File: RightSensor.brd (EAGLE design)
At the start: 19.7 x 19.7 mm, 9 parts

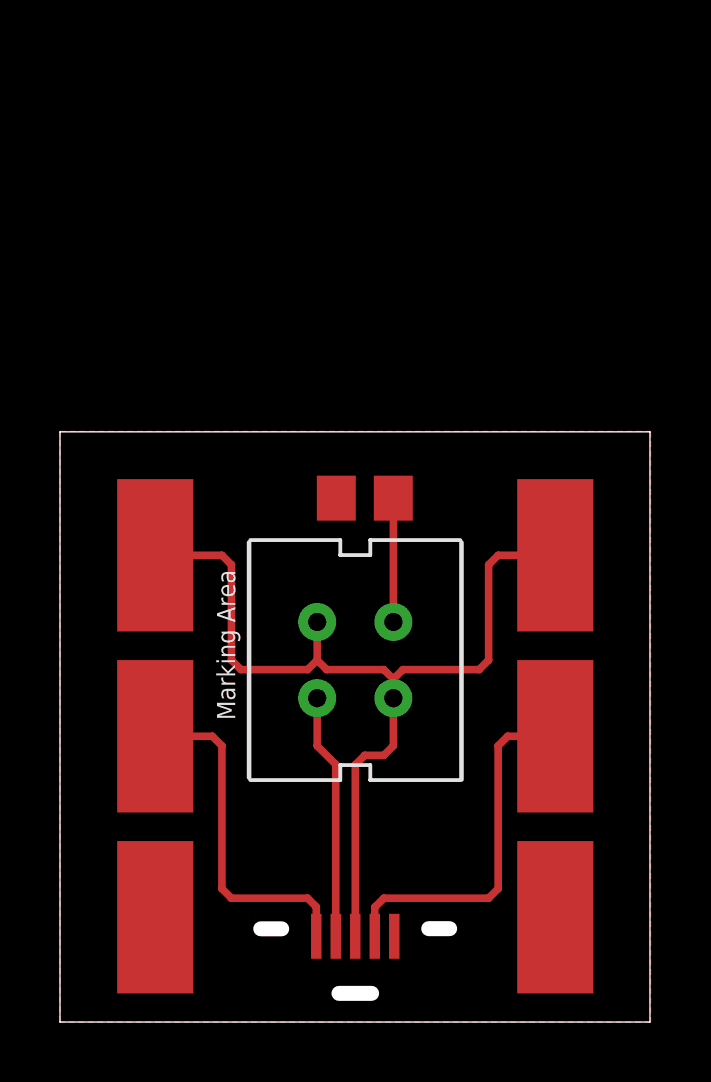
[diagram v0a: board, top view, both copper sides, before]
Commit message: Added sensor boards, started on proto frame design
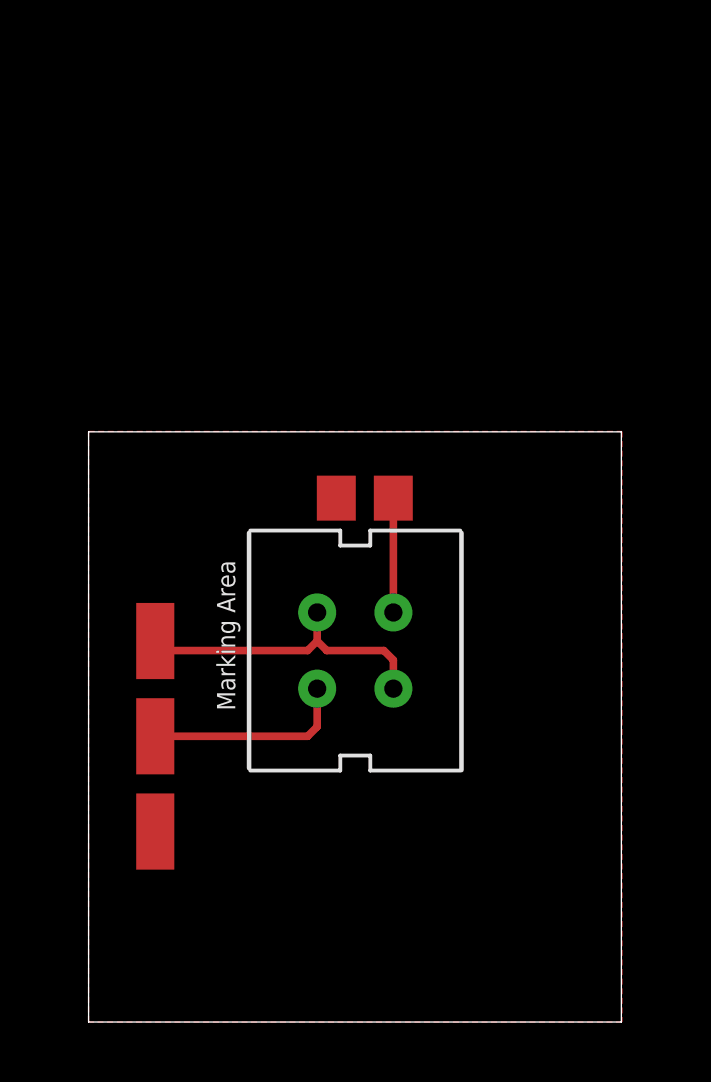
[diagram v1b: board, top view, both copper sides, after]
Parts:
- removed PAD4, PAD5, PAD6: WIREPADSMD2,54-5,08, wirepad:SMD2,54-5,08
- removed U$1: MOLES-USB-MICRO, tom:MOLEX-USB-MICRO
- removed U$2: CNY70, cny70:4
- added X2: CNY70, cny70:4
- PAD1, PAD2, PAD3: value WIREPADSMD2,54-5,08 -> WIREPADSMD1,27-254; device wirepad:SMD2,54-5,08 -> wirepad:SMD1,27-2,54
- moved PAD1 2.86 mm to (1.91, 12.7)
- moved PAD3 2.86 mm to (1.91, 6.35)
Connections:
- removed net SENSOR1: PAD2.1, U$1.VBUS
- removed net SENSOR2: U$1.D-, U$2.E
- removed net SENSOR3: PAD5.1, U$1.ID
- new net SENSOR: PAD2.1, X2.E
- net GND: no longer PAD6.1, U$1.GND
- net N$1: now also X2.K; no longer U$2.K
- net VCC: now also X2.A, X2.C; no longer PAD4.1, U$1.D+, U$2.A, U$2.C
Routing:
- net VCC: track 31.5 -> 10.4 mm
- net SENSOR3: track 12.1 -> 0.00 mm
- net SENSOR1: track 11.5 -> 0.00 mm
- net SENSOR2: track 8.19 -> 0.00 mm
- net SENSOR: track 0.00 -> 6.80 mm
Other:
- board size 19.7 x 19.7 mm -> 17.8 x 19.7 mm

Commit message: Added code V1
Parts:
- removed PAD1, PAD2, PAD3: WIREPADSMD1,27-254, wirepad:SMD1,27-2,54
- added PAD4, PAD5, PAD6: WIREPADSMD1,27-254, wirepad:SMD1,27-2,54
- moved R1 7.90 mm to (7.62, 25.3)
- moved X2 7.58 mm to (7.30, 19.9)
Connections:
- net GND: now also PAD6.1; no longer PAD3.1
- net SENSOR: now also PAD5.1; no longer PAD2.1
- net VCC: now also PAD4.1; no longer PAD1.1
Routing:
- net VCC: track 10.4 -> 13.8 mm
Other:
- board size 17.8 x 19.7 mm -> 14.6 x 22.1 mm
